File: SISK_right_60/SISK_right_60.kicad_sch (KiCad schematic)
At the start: 73 parts, among them J1 OLED_128x32, J2 Battery Conn, J3 alternative on/off SW (wired), SW1 "6", SW10 "Z", SW11 "U", SW12 "I", SW13 "O", SW14 "P", SW15 "Ü", SW16 "*", SW19 "H", SW2 "7", SW20 "J", SW21 "K", SW22 "L", SW23 "Ö", SW24 "Ä", SW25 "'", SW27 "N", SW28 "M", SW29 ";", SW3 "8", SW30 ":", SW31 "-", SW32 "shift_R", SW35 "SPACE_R", SW36 "Alt", SW37 FN, SW38 "Ctrl", SW39 FN2, SW4 "9", SW5 "0", SW6 "ß", SW7 "`", SW8 "Backspace", SW9 "Enter", U1 Nice_Nano_V2

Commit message: fixed most of issues, updated 60% version
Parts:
- removed SW39: FN2, ScottoKeebs_Hotswap:Hotswap_MX_Plated_1.25u, symbol Switch:SW_Push
- added R1, R2: 5K, Resistor_SMD:R_1206_3216Metric_Pad1.30x1.75mm_HandSolder, symbol Device:R
- added SW17: SW_push, MX_Hotswap:MX-Hotswap-1.25U, symbol Switch:SW_Push
- D1, D11, D12, D13, D16, D17, D18, D19, D2, D21, D22, D23, D24, D25, D26, D27, D28, D29, D3, D30, D31, D32, D33, D34, D35, D36, D37, D38, D39, D41, D42, D43, D44, D8: MPN (none) -> 1N4148W
- J1: Label (none) -> OLED 128x32px; MPN (none) -> OLED 128x32 i2C
- J2: value Battery Conn -> Conn; Label (none) -> Battery Conn; MPN (none) -> S2B-PH-K-S(LF)(SN)
- J3: value alternative on/off SW (wired) -> SWITCH; Label (none) -> alt. ON/OFF Sw; MPN (none) -> not known yet
- SW-ONOFF-01: value onboard ON/OFF SW -> ~; Label (none) -> onboard ON/OFF SW; MPN (none) -> MSK12C01
- SW1: value "6" -> SW_push; footprint ScottoKeebs_Hotswap:Hotswap_MX_Plated_1.00u -> MX_Hotswap:MX-Hotswap-1U; Label (none) -> 6; MPN (none) -> CPG151101S11
- SW10: value "Z" -> SW_push; footprint ScottoKeebs_Hotswap:Hotswap_MX_Plated_1.00u -> MX_Hotswap:MX-Hotswap-1U; Label (none) -> Z; MPN (none) -> CPG151101S11
- SW11: value "U" -> SW_push; footprint ScottoKeebs_Hotswap:Hotswap_MX_Plated_1.00u -> MX_Hotswap:MX-Hotswap-1U; Label (none) -> U; MPN (none) -> CPG151101S11
- SW12: value "I" -> SW_push; footprint ScottoKeebs_Hotswap:Hotswap_MX_Plated_1.00u -> MX_Hotswap:MX-Hotswap-1U; Label (none) -> I; MPN (none) -> CPG151101S11
- SW13: value "O" -> SW_push; footprint ScottoKeebs_Hotswap:Hotswap_MX_Plated_1.00u -> MX_Hotswap:MX-Hotswap-1U; Label (none) -> O; MPN (none) -> CPG151101S11
- SW14: value "P" -> SW_push; footprint ScottoKeebs_Hotswap:Hotswap_MX_Plated_1.00u -> MX_Hotswap:MX-Hotswap-1U; Label (none) -> P; MPN (none) -> CPG151101S11
- SW15: value "Ü" -> SW_push; footprint ScottoKeebs_Hotswap:Hotswap_MX_Plated_1.00u -> MX_Hotswap:MX-Hotswap-1U; Label (none) -> Ü; MPN (none) -> CPG151101S11
- SW16: value "*" -> SW_push; footprint ScottoKeebs_Hotswap:Hotswap_MX_Plated_1.00u -> MX_Hotswap:MX-Hotswap-1U; Label (none) -> "*"; MPN (none) -> CPG151101S11
- SW19: value "H" -> SW_push; footprint ScottoKeebs_Hotswap:Hotswap_MX_Plated_1.00u -> MX_Hotswap:MX-Hotswap-1U; Label (none) -> H; MPN (none) -> CPG151101S11
- SW2: value "7" -> SW_push; footprint ScottoKeebs_Hotswap:Hotswap_MX_Plated_1.00u -> MX_Hotswap:MX-Hotswap-1U; Label (none) -> 7; MPN (none) -> CPG151101S11
- SW20: value "J" -> SW_push; footprint ScottoKeebs_Hotswap:Hotswap_MX_Plated_1.00u -> MX_Hotswap:MX-Hotswap-1U; Label (none) -> J; MPN (none) -> CPG151101S11
- SW21: value "K" -> SW_push; footprint ScottoKeebs_Hotswap:Hotswap_MX_Plated_1.00u -> MX_Hotswap:MX-Hotswap-1U; Label (none) -> K; MPN (none) -> CPG151101S11
- SW22: value "L" -> SW_push; footprint ScottoKeebs_Hotswap:Hotswap_MX_Plated_1.00u -> MX_Hotswap:MX-Hotswap-1U; Label (none) -> L; MPN (none) -> CPG151101S11
- SW23: value "Ö" -> SW_push; footprint ScottoKeebs_Hotswap:Hotswap_MX_Plated_1.00u -> MX_Hotswap:MX-Hotswap-1U; Label (none) -> Ö; MPN (none) -> CPG151101S11
- SW24: value "Ä" -> SW_push; footprint ScottoKeebs_Hotswap:Hotswap_MX_Plated_1.00u -> MX_Hotswap:MX-Hotswap-1U; Label (none) -> Ä; MPN (none) -> CPG151101S11
- SW25: value "'" -> SW_push; footprint ScottoKeebs_Hotswap:Hotswap_MX_Plated_1.00u -> MX_Hotswap:MX-Hotswap-1U; Label (none) -> "'"; MPN (none) -> CPG151101S11
- SW27: value "N" -> SW_push; footprint ScottoKeebs_Hotswap:Hotswap_MX_Plated_1.00u -> MX_Hotswap:MX-Hotswap-1U; Label (none) -> N; MPN (none) -> CPG151101S11
- SW28: value "M" -> SW_push; footprint ScottoKeebs_Hotswap:Hotswap_MX_Plated_1.00u -> MX_Hotswap:MX-Hotswap-1U; Label (none) -> M; MPN (none) -> CPG151101S11
- SW29: value ";" -> SW_push; footprint ScottoKeebs_Hotswap:Hotswap_MX_Plated_1.00u -> MX_Hotswap:MX-Hotswap-1U; Label (none) -> ";"; MPN (none) -> CPG151101S11
- SW3: value "8" -> SW_push; footprint ScottoKeebs_Hotswap:Hotswap_MX_Plated_1.00u -> MX_Hotswap:MX-Hotswap-1U; Label (none) -> 8; MPN (none) -> CPG151101S11
- SW30: value ":" -> SW_push; footprint ScottoKeebs_Hotswap:Hotswap_MX_Plated_1.00u -> MX_Hotswap:MX-Hotswap-1U; Label (none) -> ":"; MPN (none) -> CPG151101S11
- SW31: value "-" -> SW_push; footprint ScottoKeebs_Hotswap:Hotswap_MX_Plated_1.00u -> MX_Hotswap:MX-Hotswap-1U; Label (none) -> "-"; MPN (none) -> CPG151101S11
- SW32: value "shift_R" -> SW_push; footprint ScottoKeebs_Hotswap:Hotswap_MX_Plated_2.75u -> MX_Hotswap:MX-Hotswap-2.75U; Label (none) -> Shift R; MPN (none) -> CPG151101S11
- SW35: value "SPACE_R" -> SW_push; footprint ScottoKeebs_Hotswap:Hotswap_MX_Plated_2.75u -> MX_Hotswap:MX-Hotswap-2.75U; Label (none) -> Space R; MPN (none) -> CPG151101S11
- SW36: value "Alt" -> SW_push; footprint ScottoKeebs_Hotswap:Hotswap_MX_Plated_1.25u -> MX_Hotswap:MX-Hotswap-1.25U; Label (none) -> Alt; MPN (none) -> CPG151101S11
- SW37: value FN -> SW_push; footprint ScottoKeebs_Hotswap:Hotswap_MX_Plated_1.25u -> MX_Hotswap:MX-Hotswap-1.25U; Label (none) -> Fn; MPN (none) -> CPG151101S11
- SW38: value "Ctrl" -> SW_push; footprint ScottoKeebs_Hotswap:Hotswap_MX_Plated_1.25u -> MX_Hotswap:MX-Hotswap-1.25U; Label (none) -> Ctrl; MPN (none) -> CPG151101S11
- SW4: value "9" -> SW_push; footprint ScottoKeebs_Hotswap:Hotswap_MX_Plated_1.00u -> MX_Hotswap:MX-Hotswap-1U; Label (none) -> 9; MPN (none) -> CPG151101S11
- SW5: value "0" -> SW_push; footprint ScottoKeebs_Hotswap:Hotswap_MX_Plated_1.00u -> MX_Hotswap:MX-Hotswap-1U; Label (none) -> 0; MPN (none) -> CPG151101S11
- SW6: value "ß" -> SW_push; footprint ScottoKeebs_Hotswap:Hotswap_MX_Plated_1.00u -> MX_Hotswap:MX-Hotswap-1U; Label (none) -> ß; MPN (none) -> CPG151101S11
- SW7: value "`" -> SW_push; footprint ScottoKeebs_Hotswap:Hotswap_MX_Plated_1.00u -> MX_Hotswap:MX-Hotswap-1U; Label (none) -> "`"; MPN (none) -> CPG151101S11
- SW8: value "Backspace" -> SW_push; footprint ScottoKeebs_Hotswap:Hotswap_MX_Plated_2.00u -> MX_Hotswap:MX-Hotswap-2U; Label (none) -> Backspace; MPN (none) -> CPG151101S11
- SW9: value "Enter" -> SW_push; footprint ScottoKeebs_Hotswap:Hotswap_MX_Plated_ISOEnter -> MX_Hotswap:MX-Hotswap-ISO; Label (none) -> Enter; MPN (none) -> CPG151101S11
- U1: Label (none) -> Nice!NanoV2; MPN (none) -> nice!nano v2 or compatible
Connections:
- net COL4: now also SW17.1
- net at D3.2 (A): now also SW17.2
- net +VDC: now reaches J3.1 (Pin_1), SW-ONOFF-01.1 (A), U1.24 (B+)
- net SCL: now reaches J1.3 (SCL), U1.6 (3)
- net SCL: now also R2.2
- net SDA: now reaches J1.4 (SDA), U1.5 (2)
- net SDA: now also R1.2
- net +3.3V renamed +BATT
- net VCC renamed +3,3V
- net +3,3V: now also R1.1, R2.1
- no-connect marks 9 -> 6
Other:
- moved on the sheet: D8, J1, J2, J3, SW35

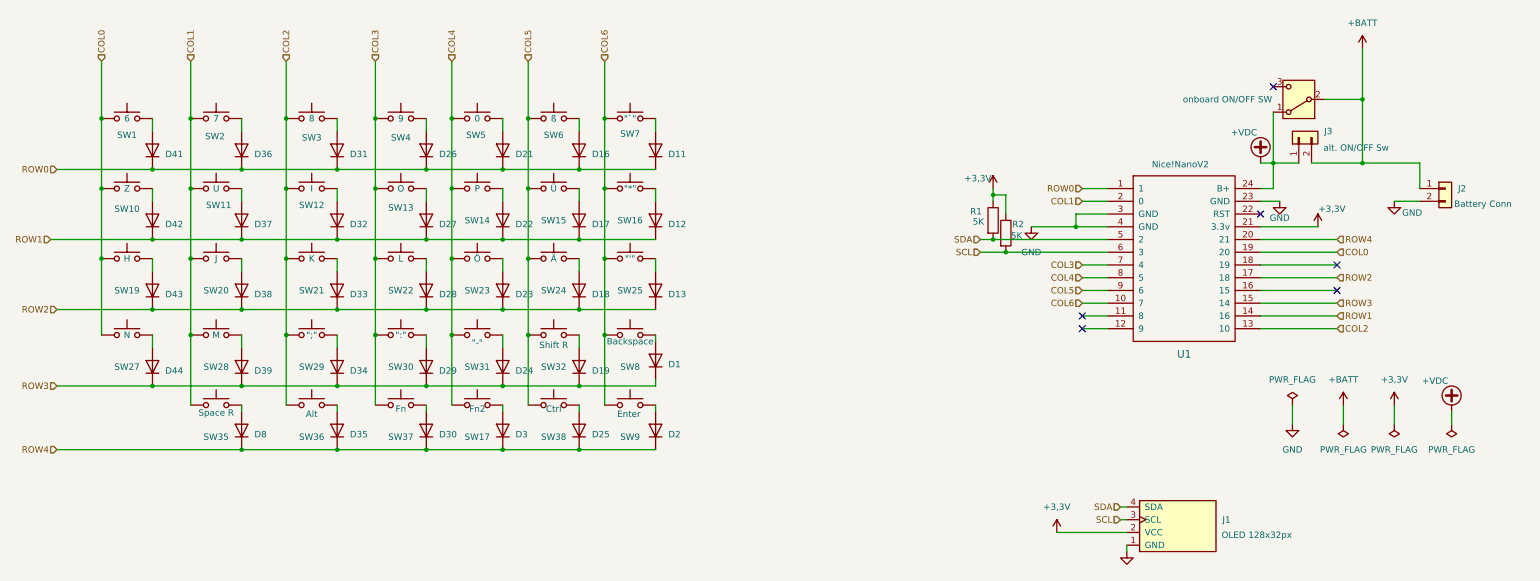
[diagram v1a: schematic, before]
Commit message: improved the whole mounting hole situation
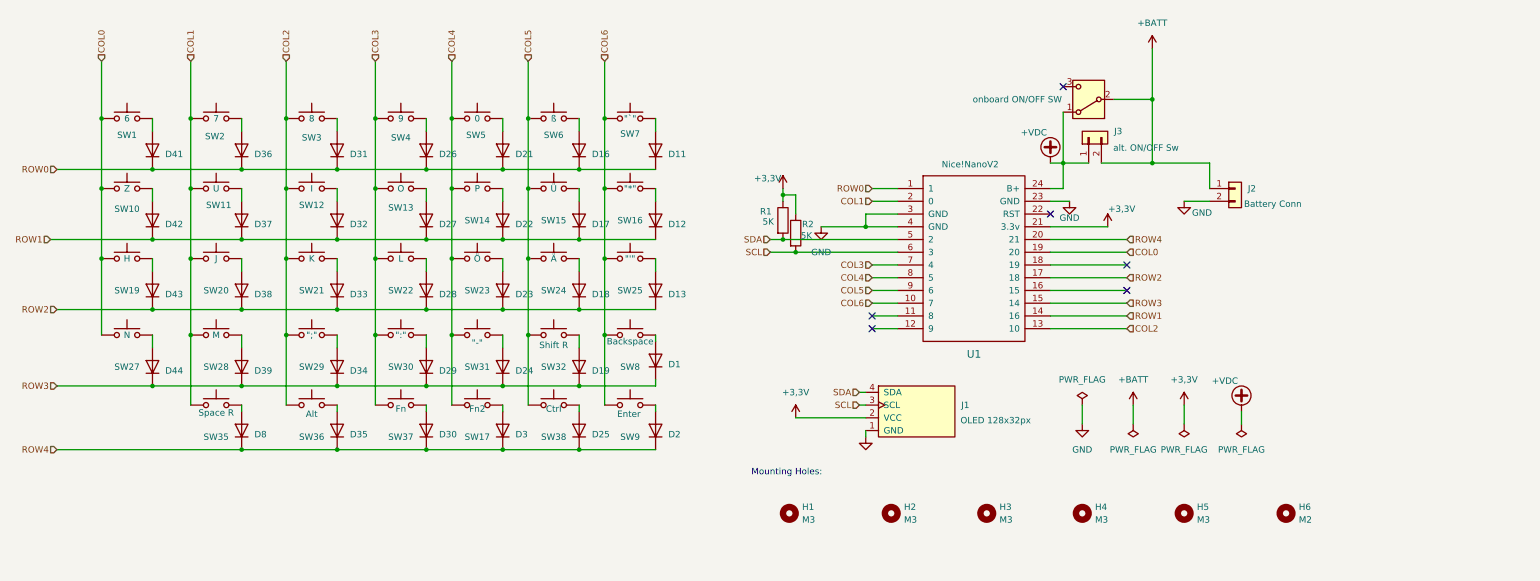
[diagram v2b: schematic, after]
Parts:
- added H1, H2, H3, H4, H5: M3, MountingHole:MountingHole_3.2mm_M3_ISO7380_Pad_TopBottom, symbol Mechanical:MountingHole
- added H6: M2, MountingHole:MountingHole_2.2mm_M2_ISO7380_Pad_TopOnly, symbol Mechanical:MountingHole
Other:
- note added: "Mounting Holes:"
- moved on the sheet: J1, J2, J3, R1, R2, U1

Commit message: last changes on silkscreen before manufaturing
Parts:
- SW17: Label Fn2 -> Super
- SW36: Label Alt -> Fn
- SW37: Label Fn -> Alt
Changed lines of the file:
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@@
 			)
 		)
-		(property "Label" "Alt"
+		(property "Label" "Fn"
 			(at 88.9 105.918 0)
 			(effects
@@
 			)
 		)
-		(property "Label" "Fn"
+		(property "Label" "Alt"
 			(at 106.68 104.14 0)
 			(effects
@@
 			)
 		)
-		(property "Label" "Fn2"
+		(property "Label" "Super"
 			(at 121.92 104.14 0)
 			(effects
